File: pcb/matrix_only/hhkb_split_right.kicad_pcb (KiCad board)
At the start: 2 copper layers, 173.7 x 97.4 mm, 83 parts, among them SW1 CPG151101S11-2, SW10 CPG151101S11-2, SW11 CPG151101S11-2, SW12 CPG151101S11-2, SW13 CPG151101S11-2, SW14 CPG151101S11-2, SW15 CPG151101S11-2, SW16 CPG151101S11-2, SW17 CPG151101S11-2, SW18 CPG151101S11-2, SW19 CPG151101S11-2, SW2 CPG151101S11-2, SW20 CPG151101S11-2, SW21 CPG151101S11-2, SW22 CPG151101S11-2, SW23 CPG151101S11-2, SW24 CPG151101S11-2, SW25 CPG151101S11-2, SW26 CPG151101S11-2, SW27 CPG151101S11-2, SW28 CPG151101S11-2, SW29 CPG151101S11-2, SW3 CPG151101S11-2, SW30 CPG151101S11-2, SW31 CPG151101S11-2, SW32 CPG151101S11-2, SW33 CPG151101S11-2, SW34 CPG151101S11-2, SW4 CPG151101S11-2, SW5 CPG151101S11-2, SW6 CPG151101S11-2, SW7 CPG151101S11-2, SW8 CPG151101S11-2, SW9 CPG151101S11-2, U1 74LVC595, U2 74LVC595

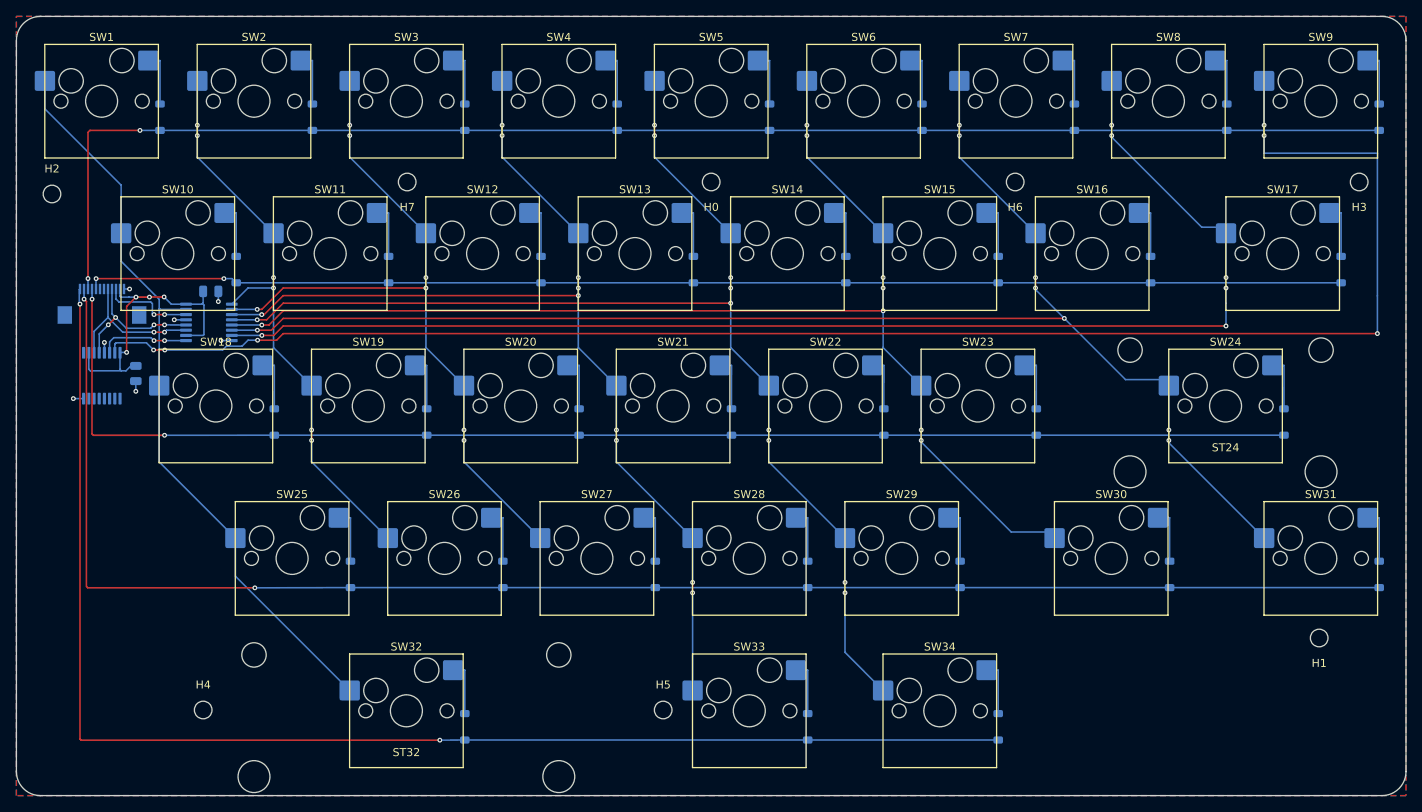
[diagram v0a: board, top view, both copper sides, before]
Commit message: #51 候補 3 を「右半分のみ」で実装した（PLATE_MARGIN_X_RIGHT = 3.125・幅 177.7mm）
利用者の採用決定を受けた実装。**左は実機のまま**——全幅で詰めると
電池（外壁基準）と子基板（内壁基準）が両側から近づき、左のアンテナ・
電池距離が 10.56→8.56mm で要件 10mm を割る（実装して発覚・巻き戻した）。
右の同距離は余裕 40mm で影響なし。実機からの逸脱も右半分だけになった。

- interface.py: 右専用余白＋margin_x()/margin_x_for_case()（キー幅 150mm/
  ケース幅 158mm を境に半分を判別。呼び出し元の変更を最小化）
- BEZEL_WALL 1.6→1.2・BEZEL_OPENING_GAP 1.5→0.9 は左右共通
  （見える隙間 1.225mm = 実機実測 1.0〜1.5 の範囲内）
- 検査: 余白の実機由来検査を左右別に・ベゼル幾何検査を両半分で実施・
  キャップ隙間の下限を実機実測の 1.0 に更新
- 右の新外形板を matrix_only に用意（利用者が J_DB 周り 9 ネットを引き直し中）
- 左基板・DRC 記録は凍結のまま無傷

検証: DRC 0/0/0（左右とも現行板で）・幾何/不変検査 138 件緑・
gen_assembly 左 干渉 0・全検査で残る赤は右基板系 3 件のみ
（旧外形の本番右板 vs 新定数。引き直し→finalize で解消する見込み）

Co-Authored-By: Claude Fable 5 <noreply@anthropic.com>
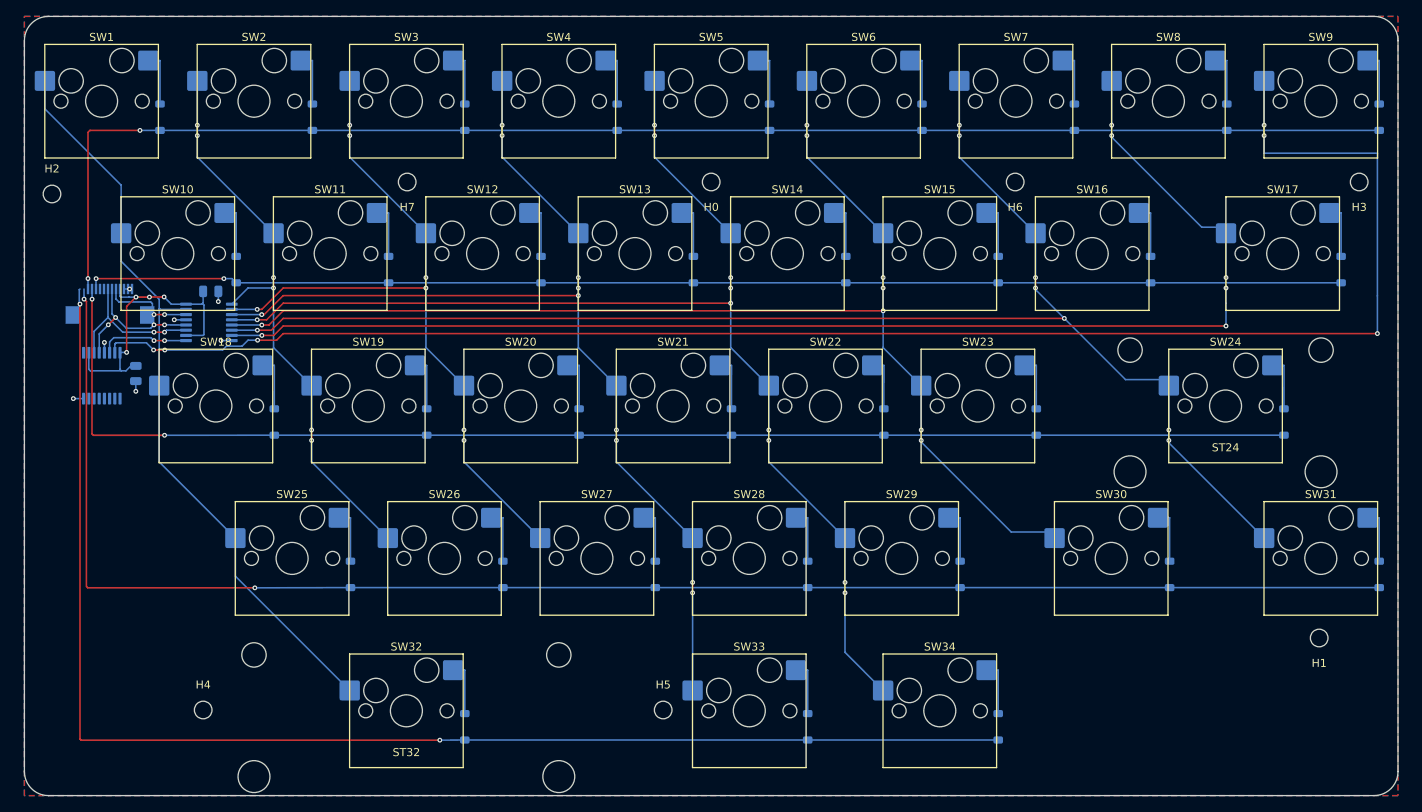
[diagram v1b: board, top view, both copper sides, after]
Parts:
- moved J_DB 1.00 mm to (74.8, 87.2)
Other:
- board size 173.7 x 97.4 mm -> 171.7 x 97.4 mm

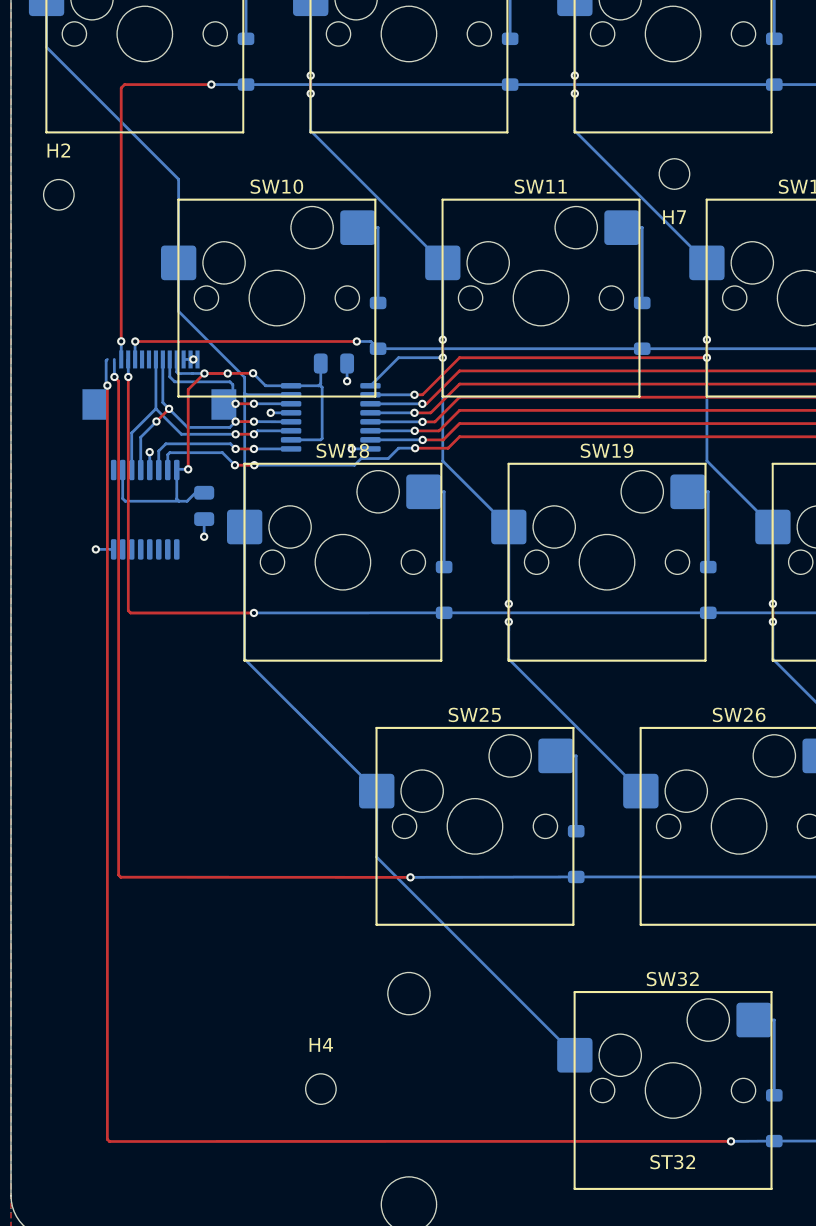
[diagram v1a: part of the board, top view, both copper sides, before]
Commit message: #51 の基板一式——3 枚とも DRC 違反 0 / 未配線 0
利用者が右の J_DB 周り 9 ネットを新しい位置へ引き直し（matrix_only）、
V3V3 の切れ目と、写しの φ0.5→0.56 化で近すぎたビア 3 ペアも修正。
写し（matrix_routing.json）→ gen_pcb（外形 左 138.4 / 右 171.7）→
finalize --src unrouted → DRC の全経路を通した。部品位置の写しを含む。

Co-Authored-By: Claude Fable 5 <noreply@anthropic.com>
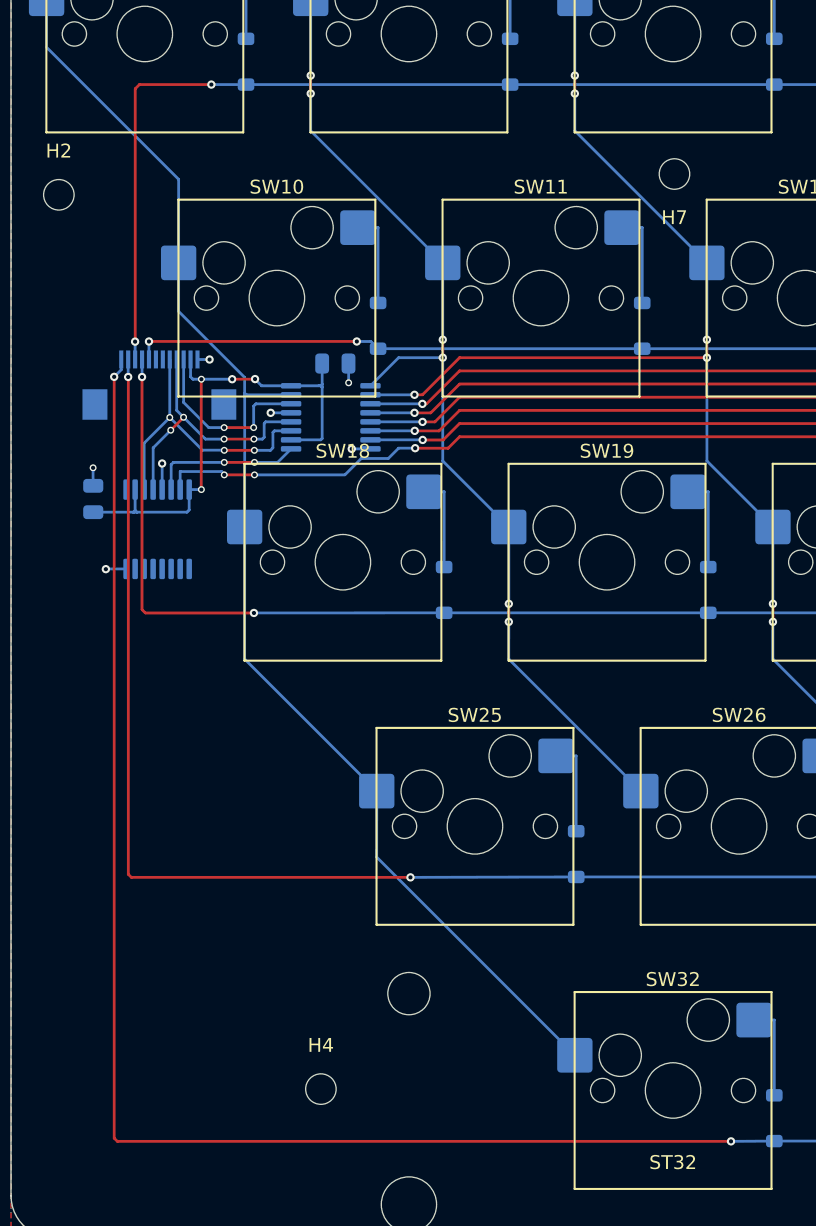
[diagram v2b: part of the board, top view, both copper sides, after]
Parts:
- moved C_U2 8.02 mm to (70.1, 95.4), turned to 90 degrees
- moved U2 1.67 mm to (74.7, 97.6)
- moved C_U1 0.10 mm to (87.5, 85.7)
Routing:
- net SPI_SCK: track 19.3 -> 21.3 mm, vias 2 -> 3
- net V3V3: track 40.0 -> 38.1 mm
- net SPI_MOSI: track 11.6 -> 13.2 mm
- net CS: track 18.5 -> 20.0 mm
- net GND: track 8.65 -> 9.74 mm
- net ROW_C: track 181.1 -> 180.0 mm
- net ROW_B: track 167.2 -> 166.1 mm
- net ROW_A: track 157.1 -> 156.1 mm
- net ROW_D: track 199.0 -> 198.1 mm
- net COL8: track 206.0 -> 205.2 mm

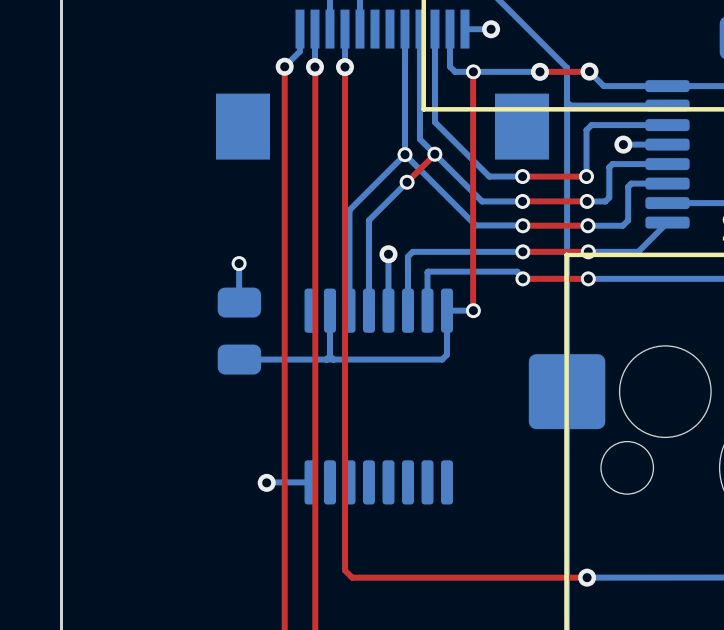
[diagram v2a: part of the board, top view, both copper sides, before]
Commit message: C_U2 の寄せ（利用者）を取り込み、番人 MAX_DECOUPLE_MM を根拠つきで 6.5 へ——**全検査 458 件緑**
利用者が C_U2 を U2 の干渉限界まで寄せ（7.11 → 6.21mm）シルクも修正。
上限 6.0 は「物理から決まらない・17mm 再発防止の番人」と自ら明記された
経験則なので、実配置 6.21 + 余裕 0.3 = 6.5 へ更新（全ペアの現状:
左 C_U1 4.97 / 右 C_U1 2.76 / 右 C_U2 6.21）。

これで #51 関連の作業は完了:
- 3 基板とも DRC 違反 0 / 未配線 0
- 実形状の組み立て干渉 左右 0
- 全検査 458 件緑・skip 9

Co-Authored-By: Claude Fable 5 <noreply@anthropic.com>
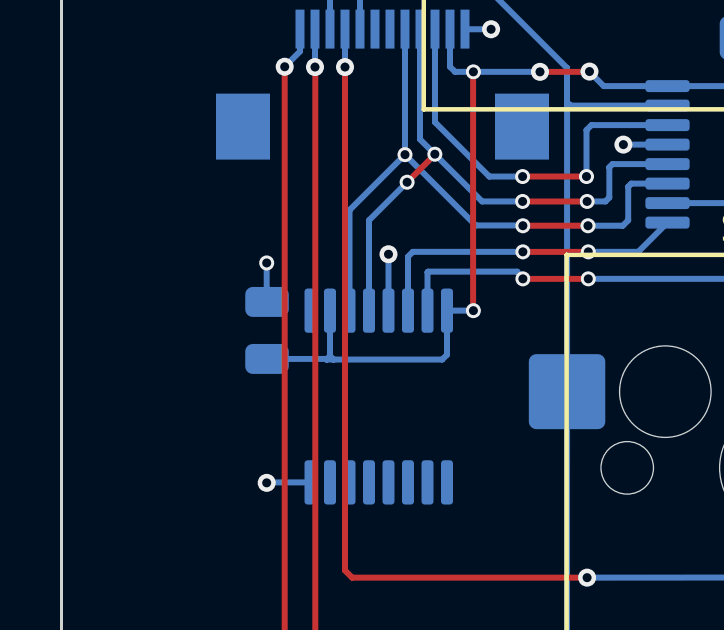
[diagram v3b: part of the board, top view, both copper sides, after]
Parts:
- moved C_U2 0.92 mm to (71.0, 95.4)
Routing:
- net V3V3: track 38.1 -> 37.2 mm
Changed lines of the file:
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@@
 		(tags "TSSOP SO JEDEC-MO-153-AB Texas_PW0016A Microchip-ST Toshiba-TSSOP16-P-0044-0.65A NXP-SOT403-1 Infineon-P-TSSOP-16-800")
 		(property "Reference" "U2"
-			(at 0 -4.27 270)
+			(at -5.1875 0.005 270)
 			(layer "B.SilkS")
 			(effects
@@
 	(footprint "C_0805_2012Metric"
 		(layer "B.Cu")
-		(at 70.08 95.44 90)
+		(at 71 95.42 90)
 		(descr "Capacitor SMD 0805 (2012 Metric), square (rectangular) end terminal, IPC-7351 nominal, (Body size source: IPC-SM-782 page 76, https://www.pcb-3d.com/wordpress/wp-content/uploads/ipc-sm-782a_amendment_1_and_2.pdf, https://docs.google.com/spreadsheets/d/1BsfQQcO9C6DZCsRaXUlFlo91Tg2WpOkGARC1WS5S8t0/edit?usp=sharing)")
 		(tags "capacitor")
 		(property "Reference" "C_U2"
-			(at 4.61 -0.02 90)
+			(at 0 -1.72 90)
 			(layer "B.SilkS")
 			(effects
@@
 	)
 	(segment
-		(start 72.98 96.39)
-		(end 70.08 96.39)
+		(start 72.98 96.37)
+		(end 71 96.37)
 		(width 0.2)
 		(layer "B.Cu")
@@
 	)
 	(segment
+		(start 72.99 96.38)
+		(end 72.98 96.37)
+		(width 0.2)
+		(layer "B.Cu")
+		(net "V3V3")
+	)
+	(segment
 		(start 72.99 96.39)
 		(end 73.22 96.39)
@@
 	)
 	(via
-		(at 70.07 93.19)
+		(at 70.99 93.17)
 		(size 0.5)
 		(drill 0.3)
@@
 	)
 	(segment
-		(start 70.07 94.48)
-		(end 70.08 94.49)
-		(width 0.2)
-		(layer "B.Cu")
-		(net "GND")
-	)
-	(segment
 		(start 78.47 85.38)
 		(end 77.604999 85.38)
@@
 	)
 	(segment
-		(start 70.07 93.19)
-		(end 70.07 94.48)
+		(start 70.99 93.17)
+		(end 70.99 94.46)
 		(width 0.2)
 		(layer "B.Cu")

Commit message: #49 SPARE/SPARE2（XIAO D4/D9）を主基板で露出——I2C などの拡張用。右の J_DB 周りのビアを φ0.6 に統一
- 利用者が matrix_only で J_DB パッド 6・7 から枝＋ビアを手で打った（左右）
- pcb_rules.DEBUG_NETS に 2 ネットを追加、finalize_pcb で本番へ
- 右の φ0.5/0.3 ビア 17 個（アニュラー 0.10 < 0.13）を φ0.6 に揃え、違反 17 → 0
- DRC 3 枚 違反 0 / 未配線 0。検査 151 緑。export_fab リハーサル通過（B.Mask 開口 4 点確認）
- 記録: open-gaps #49・fab-checklist 4b・pcb_parts / product_groups

Co-Authored-By: Claude Fable 5 <noreply@anthropic.com>
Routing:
- net SPARE2: track 0.00 -> 2.45 mm, vias 0 -> 1
- net SPARE: track 0.00 -> 2.27 mm, vias 0 -> 1
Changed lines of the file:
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@@
 	(via
 		(at 79.53 93.7)
-		(size 0.5)
+		(size 0.6)
 		(drill 0.3)
 		(layers "F.Cu" "B.Cu")
@@
 	(via
 		(at 81.71 93.7)
-		(size 0.5)
+		(size 0.6)
 		(drill 0.3)
 		(layers "F.Cu" "B.Cu")
@@
 	(via
 		(at 77.88 86.8)
-		(size 0.5)
+		(size 0.6)
 		(drill 0.3)
 		(layers "F.Cu" "B.Cu")
@@
 	(via
 		(at 77.88 94.76)
-		(size 0.5)
+		(size 0.6)
 		(drill 0.3)
 		(layers "F.Cu" "B.Cu")
@@
 	(via
 		(at 70.99 93.17)
-		(size 0.5)
+		(size 0.6)
 		(drill 0.3)
 		(layers "F.Cu" "B.Cu")
@@
 	(via
 		(at 88.5 87.06)
-		(size 0.5)
+		(size 0.6)
 		(drill 0.3)
 		(layers "F.Cu" "B.Cu")
@@
 	(via
 		(at 79.53 91.93)
-		(size 0.5)
+		(size 0.6)
 		(drill 0.3)
 		(layers "F.Cu" "B.Cu")
@@
 	(via
 		(at 75.599999 89.559999)
-		(size 0.5)
+		(size 0.6)
 		(drill 0.3)
 		(layers "F.Cu" "B.Cu")
@@
 	(via
 		(at 81.7 91.93)
-		(size 0.5)
+		(size 0.6)
 		(drill 0.3)
 		(layers "F.Cu" "B.Cu")
@@
 	(via
 		(at 79.52 91.12)
-		(size 0.5)
+		(size 0.6)
 		(drill 0.3)
 		(layers "F.Cu" "B.Cu")
@@
 	(via
 		(at 76.595 89.545)
-		(size 0.5)
+		(size 0.6)
 		(drill 0.3)
 		(layers "F.Cu" "B.Cu")
@@
 	(via
 		(at 81.67 91.12)
-		(size 0.5)
+		(size 0.6)
 		(drill 0.3)
 		(layers "F.Cu" "B.Cu")
@@
 	(via
 		(at 75.670735 90.479265)
-		(size 0.5)
+		(size 0.6)
 		(drill 0.3)
 		(layers "F.Cu" "B.Cu")
@@
 	(via
 		(at 79.53 92.8)
-		(size 0.5)
+		(size 0.6)
 		(drill 0.3)
 		(layers "F.Cu" "B.Cu")
@@
 	(via
 		(at 81.71 92.8)
-		(size 0.5)
+		(size 0.6)
 		(drill 0.3)
 		(layers "F.Cu" "B.Cu")
@@
 	(via
 		(at 79.52 90.29)
-		(size 0.5)
+		(size 0.6)
 		(drill 0.3)
 		(layers "F.Cu" "B.Cu")
@@
 	(via
 		(at 81.65 90.29)
-		(size 0.5)
+		(size 0.6)
 		(drill 0.3)
 		(layers "F.Cu" "B.Cu")
@@
 		(net "SPI_MOSI")
 	)
+	(via
+		(at 75.61 83.14)
+		(size 0.6)
+		(drill 0.3)
+		(layers "F.Cu" "B.Cu")
+		(net "SPARE2")
+	)
+	(segment
+		(start 75.099999 84.460001)
+		(end 75.6 83.96)
+		(width 0.2)
+		(layer "B.Cu")
+		(net "SPARE2")
+	)
+	(segment
+		(start 75.099999 85.375)
+		(end 75.099999 84.460001)
+		(width 0.2)
+		(layer "B.Cu")
+		(net "SPARE2")
+	)
+	(segment
+		(start 75.6 83.15)
+		(end 75.61 83.14)
+		(width 0.2)
+		(layer "B.Cu")
+		(net "SPARE2")
+	)
+	(segment
+		(start 75.6 83.96)
+		(end 75.6 83.15)
+		(width 0.2)
+		(layer "B.Cu")
+		(net "SPARE2")
+	)
+	(via
+		(at 74.69 83.15)
+		(size 0.6)
+		(drill 0.3)
+		(layers "F.Cu" "B.Cu")
+		(net "SPARE")
+	)
+	(segment
+		(start 74.599999 84.42853)
+		(end 74.7 84.328529)
+		(width 0.2)
+		(layer "B.Cu")
+		(net "SPARE")
+	)
+	(segment
+		(start 74.599999 85.375)
+		(end 74.599999 84.42853)
+		(width 0.2)
+		(layer "B.Cu")
+		(net "SPARE")
+	)
+	(segment
+		(start 74.7 84.328529)
+		(end 74.7 83.15)
+		(width 0.2)
+		(layer "B.Cu")
+		(net "SPARE")
+	)
 	(zone

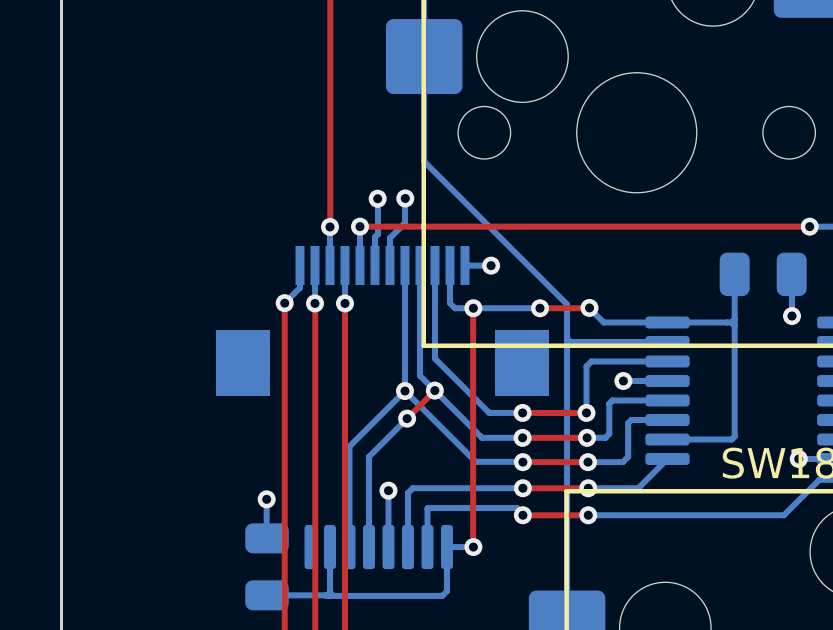
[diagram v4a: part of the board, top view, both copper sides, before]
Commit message: #19 J_DB の口を奥向きに回した（FFC は直線・A タイプで正しい）。左は配線無傷で DRC 0、右は J_DB 周りの引き直し待ち
- 原因: 2026-08-08 の初回配置で Flip() の副作用の 180° をそのまま使い、誰も口の向きを決めていなかった（git 履歴で確認）
- circuit.py: J_DB のピン表を J_MAIN の鏡像（n ↔ 13-n）に。裏面で 180° 回すとピン 1 の側が入れ替わるため。検査 2 本と決定文書を鏡像に更新
- gen_pcb.py: J_DB に向き 0° と dy（左 -3.7 / 右 -0.4）。配置は matrix_only の現物が優先
- 左 matrix_only: J_DB を 0°・3.7mm 奥へ → 12 パッドが同じ座標に戻り配線無傷。DRC 0/0
- 右 matrix_only: 3.7mm は SW10 の NPTH がコートヤードに入るため 0.4mm 止まり。パッドが南側の枝と重なり DRC 違反 20・未配線 8（利用者の引き直し・open-gaps #19 に手順）
- gen_assembly.py: 幕と床走行を消し、口の直後の潜り＋J_MAIN までの斜めのリボンに。箱モード干渉 0
- 回路図・部品記録・DRC 記録・証拠ページを更新。検査 455 緑・5 赤（全部右の引き直しと露出ビアの打ち直しに帰着・open-gaps に列挙）

Co-Authored-By: Claude Fable 5 <noreply@anthropic.com>
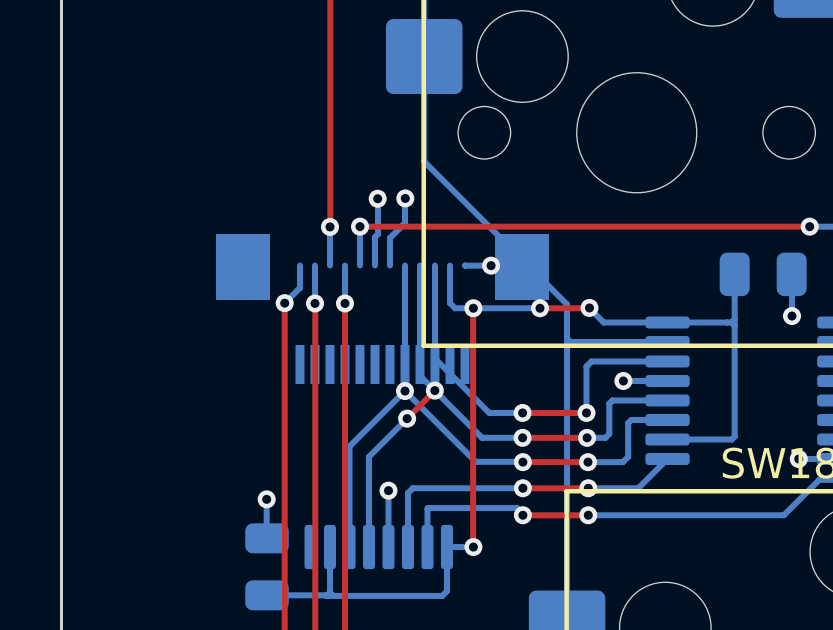
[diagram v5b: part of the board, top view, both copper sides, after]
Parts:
- moved J_DB 0.40 mm to (74.8, 86.8), turned to 0 degrees
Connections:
- J_DB pad 1: GND -> ROW_E
- J_DB pad 10: ROW_C -> SPI_MOSI
- J_DB pad 11: ROW_D -> V3V3
- J_DB pad 12: ROW_E -> GND
- J_DB pad 2: V3V3 -> ROW_D
- J_DB pad 3: SPI_MOSI -> ROW_C
- J_DB pad 4: CS -> ROW_B
- J_DB pad 5: SPI_SCK -> ROW_A
- J_DB pad 6: SPARE2 -> SPARE
- J_DB pad 7: SPARE -> SPARE2
- J_DB pad 8: ROW_A -> SPI_SCK
- J_DB pad 9: ROW_B -> CS
